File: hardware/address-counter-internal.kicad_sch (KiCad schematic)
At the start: 10 parts, among them U3 74LV163, U4 74LV163, U5 74LV163, U6 74LV163, U7 74LV163

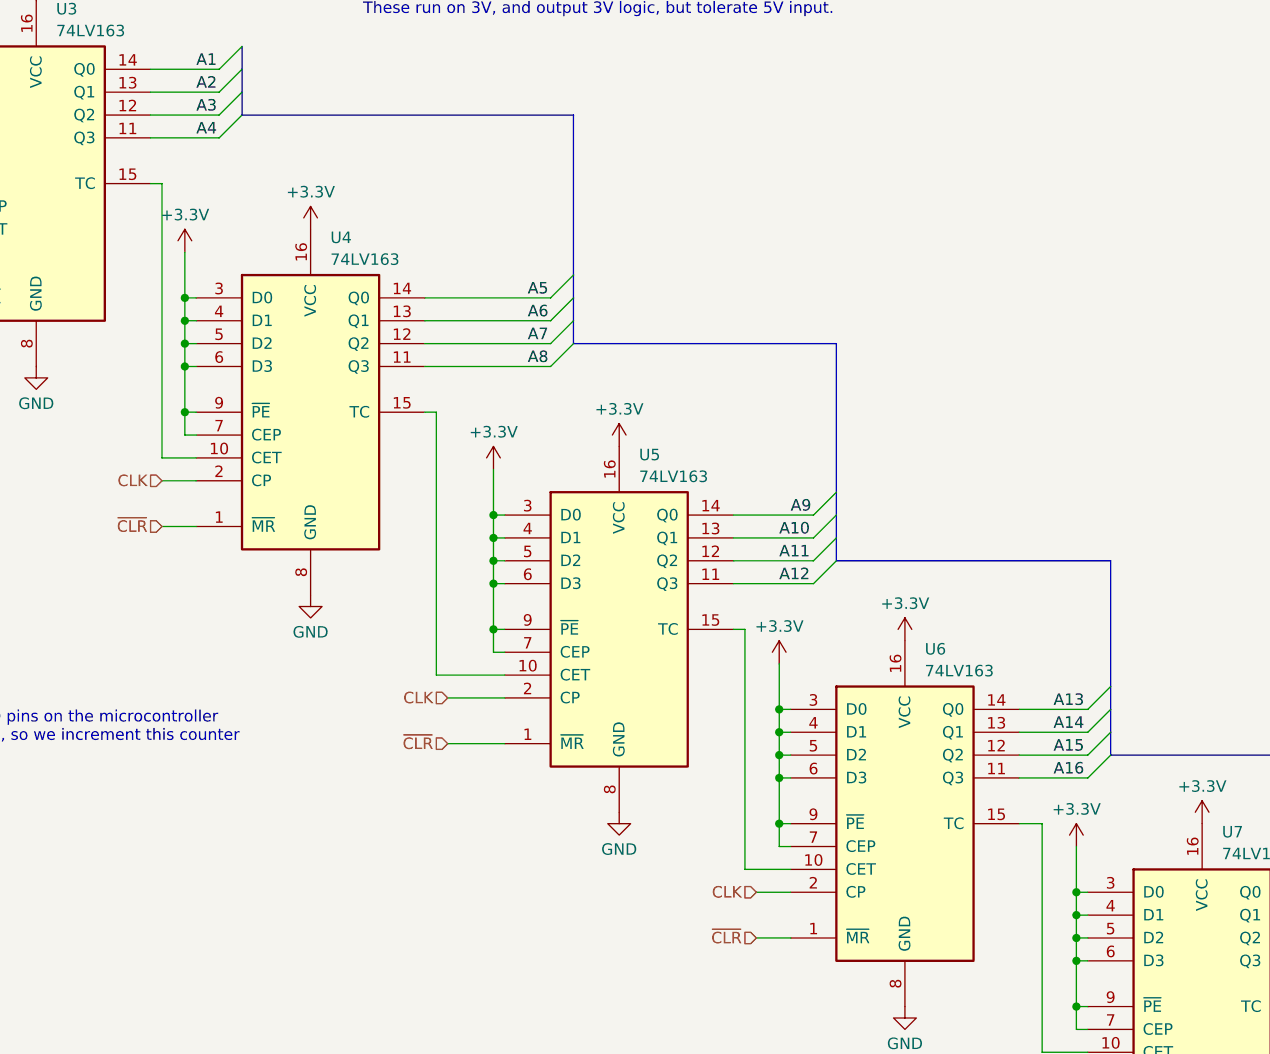
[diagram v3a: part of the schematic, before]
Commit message: Simplify microcontroller board BOM
Replace 74LV1T125 with 74LVC2G125, which simplifies the BOM by removing one special part.
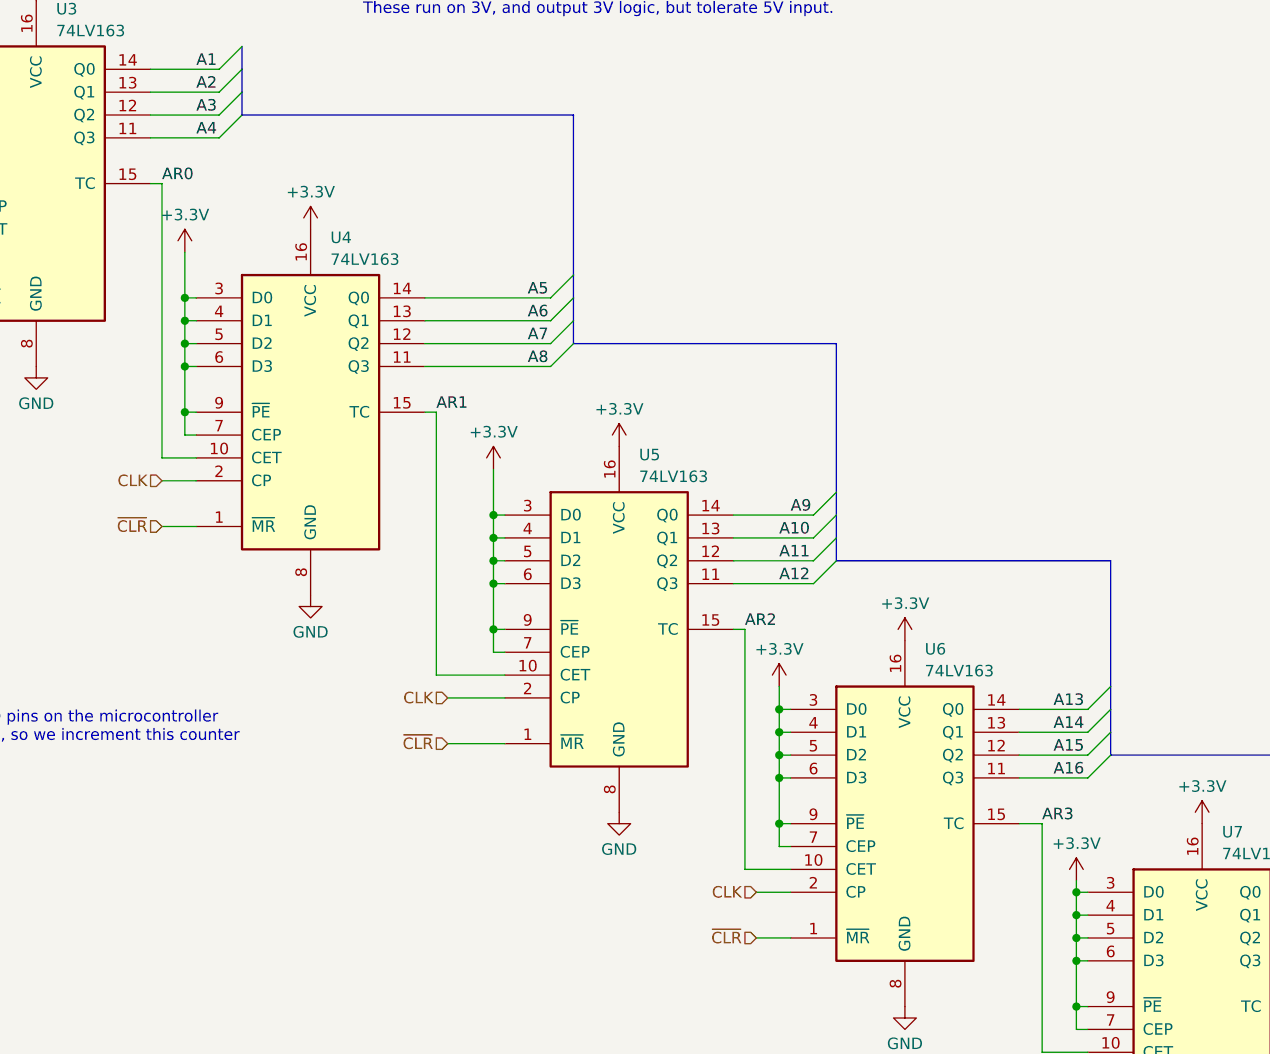
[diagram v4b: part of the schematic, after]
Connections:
- net AR0: now reaches U3.15 (TC), U4.10 (CET)
- net AR1: now reaches U4.15 (TC), U5.10 (CET)
- net AR2: now reaches U5.15 (TC), U6.10 (CET)
- net AR3: now reaches U6.15 (TC), U7.10 (CET)
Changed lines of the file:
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@@
 	(wire
 		(pts
-			(xy 163.83 115.57) (xy 163.83 120.65)
+			(xy 163.83 119.38) (xy 163.83 120.65)
 		)
 		(stroke
@@
 	(wire
 		(pts
-			(xy 130.81 95.25) (xy 130.81 100.33)
+			(xy 130.81 97.79) (xy 130.81 100.33)
 		)
 		(stroke
@@
 		)
 	)
+	(label "AR3"
+		(at 160.02 113.03 0)
+		(fields_autoplaced yes)
+		(effects
+			(font
+				(size 1.27 1.27)
+			)
+			(justify left bottom)
+		)
+	)
 	(label "A16"
 		(at 161.29 107.95 0)
@@
 		)
 	)
+	(label "AR1"
+		(at 92.71 67.31 0)
+		(fields_autoplaced yes)
+		(effects
+			(font
+				(size 1.27 1.27)
+			)
+			(justify left bottom)
+		)
+	)
 	(label "A10"
 		(at 130.81 81.28 0)
@@
 		)
 	)
+	(label "AR2"
+		(at 127 91.44 0)
+		(fields_autoplaced yes)
+		(effects
+			(font
+				(size 1.27 1.27)
+			)
+			(justify left bottom)
+		)
+	)
 	(label "A7"
 		(at 102.87 59.69 0)
@@
 	(label "A15"
 		(at 161.29 105.41 0)
+		(fields_autoplaced yes)
+		(effects
+			(font
+				(size 1.27 1.27)
+			)
+			(justify left bottom)
+		)
+	)
+	(label "AR0"
+		(at 62.23 41.91 0)
 		(fields_autoplaced yes)
 		(effects
@@
 	(symbol
 		(lib_id "power:+3.3V")
-		(at 130.81 95.25 0)
+		(at 130.81 97.79 0)
 		(unit 1)
 		(exclude_from_sim no)
@@
 		(fields_autoplaced yes)
 		(property "Reference" "#PWR038"
-			(at 130.81 99.06 0)
+			(at 130.81 101.6 0)
 			(effects
 				(font
@@
 		)
 		(property "Value" "+3.3V"
-			(at 130.81 91.1169 0)
+			(at 130.81 93.6569 0)
 			(effects
 				(font
@@
 		)
 		(property "Footprint" ""
-			(at 130.81 95.25 0)
+			(at 130.81 97.79 0)
 			(effects
 				(font
@@
 		)
 		(property "Datasheet" ""
-			(at 130.81 95.25 0)
+			(at 130.81 97.79 0)
 			(effects
 				(font
@@
 		)
 		(property "Description" "Power symbol creates a global label with name \"+3.3V\""
-			(at 130.81 95.25 0)
+			(at 130.81 97.79 0)
 			(effects
 				(font
@@
 	(symbol
 		(lib_id "power:+3.3V")
-		(at 163.83 115.57 0)
+		(at 163.83 119.38 0)
 		(unit 1)
 		(exclude_from_sim no)
@@
 		(fields_autoplaced yes)
 		(property "Reference" "#PWR039"
+			(at 163.83 123.19 0)
+			(effects
+				(font
+					(size 1.27 1.27)
+				)
+				(hide yes)
+			)
+		)
+		(property "Value" "+3.3V"
+			(at 163.83 115.2469 0)
+			(effects
+				(font
+					(size 1.27 1.27)
+				)
+			)
+		)
+		(property "Footprint" ""
 			(at 163.83 119.38 0)
 			(effects
@@
 			)
 		)
-		(property "Value" "+3.3V"
-			(at 163.83 111.4369 0)
-			(effects
-				(font
-					(size 1.27 1.27)
-				)
-			)
-		)
-		(property "Footprint" ""
-			(at 163.83 115.57 0)
-			(effects
-				(font
-					(size 1.27 1.27)
-				)
-				(hide yes)
-			)
-		)
 		(property "Datasheet" ""
-			(at 163.83 115.57 0)
+			(at 163.83 119.38 0)
 			(effects
 				(font
@@
 		)
 		(property "Description" "Power symbol creates a global label with name \"+3.3V\""
-			(at 163.83 115.57 0)
-			(effects
-				(font
+			(at 163.83 119.38 0)
+			(effects
+				(font

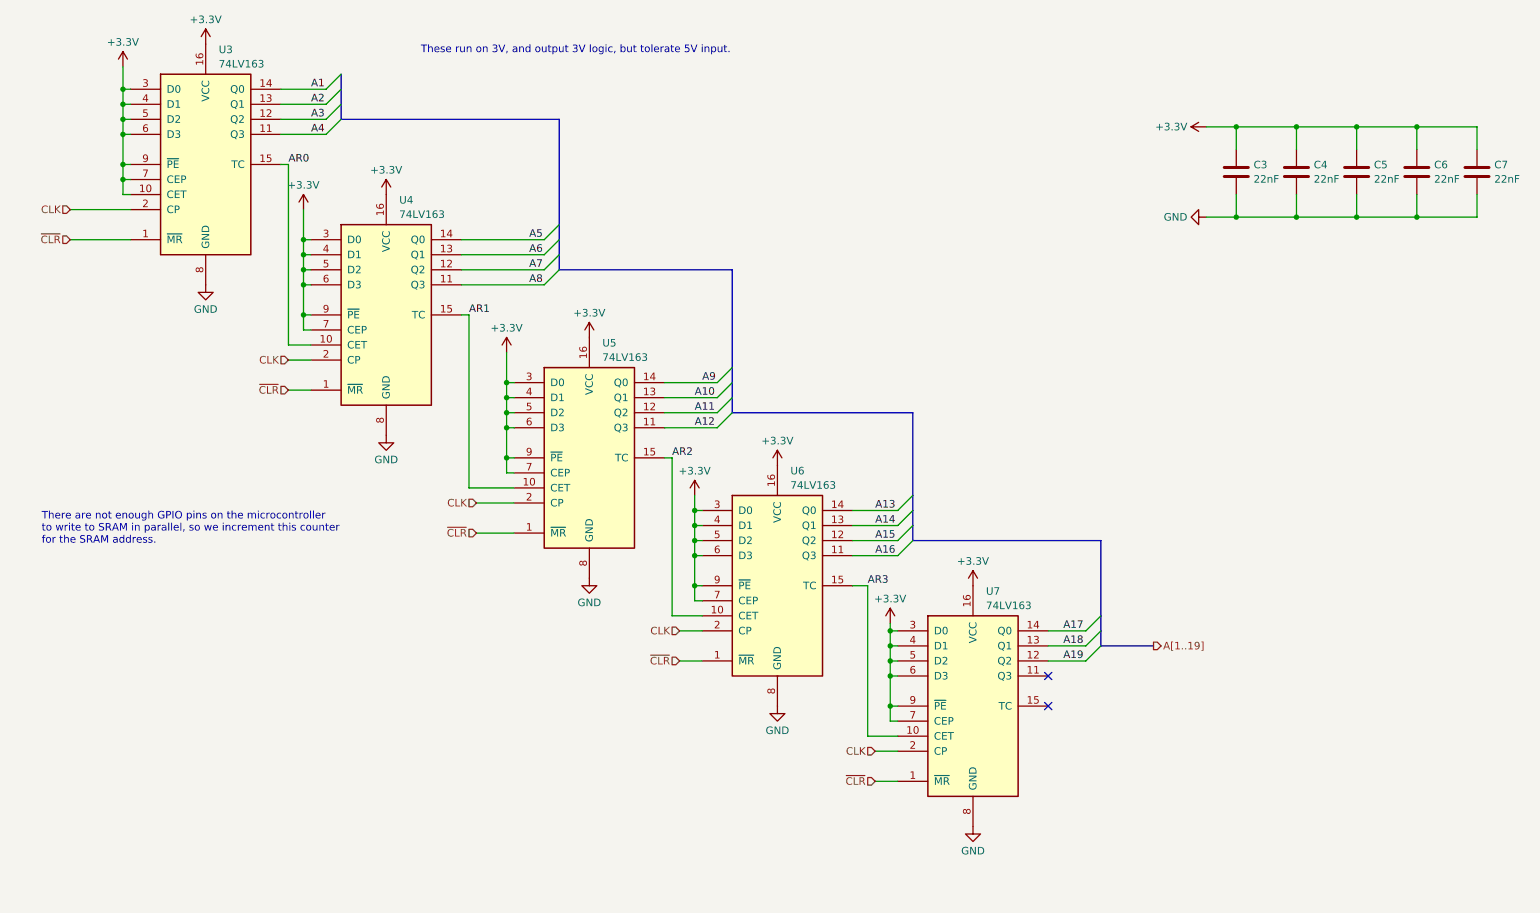
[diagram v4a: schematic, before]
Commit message: Improve uC board assembly process, fix minor bug
Changes to part numbers to better align with JLCPCB stock:
 - Replace 74LV164PW,118 / C179331 with SN74LV164APWR / C403720
 - Replace SN74LV163APWR / C2675453 with SN74LV161APWR / C2649404
   - Original had sync clear, but this is async clear, which is a bug
     fix!
 - Fix rotation of U8, U9, U13
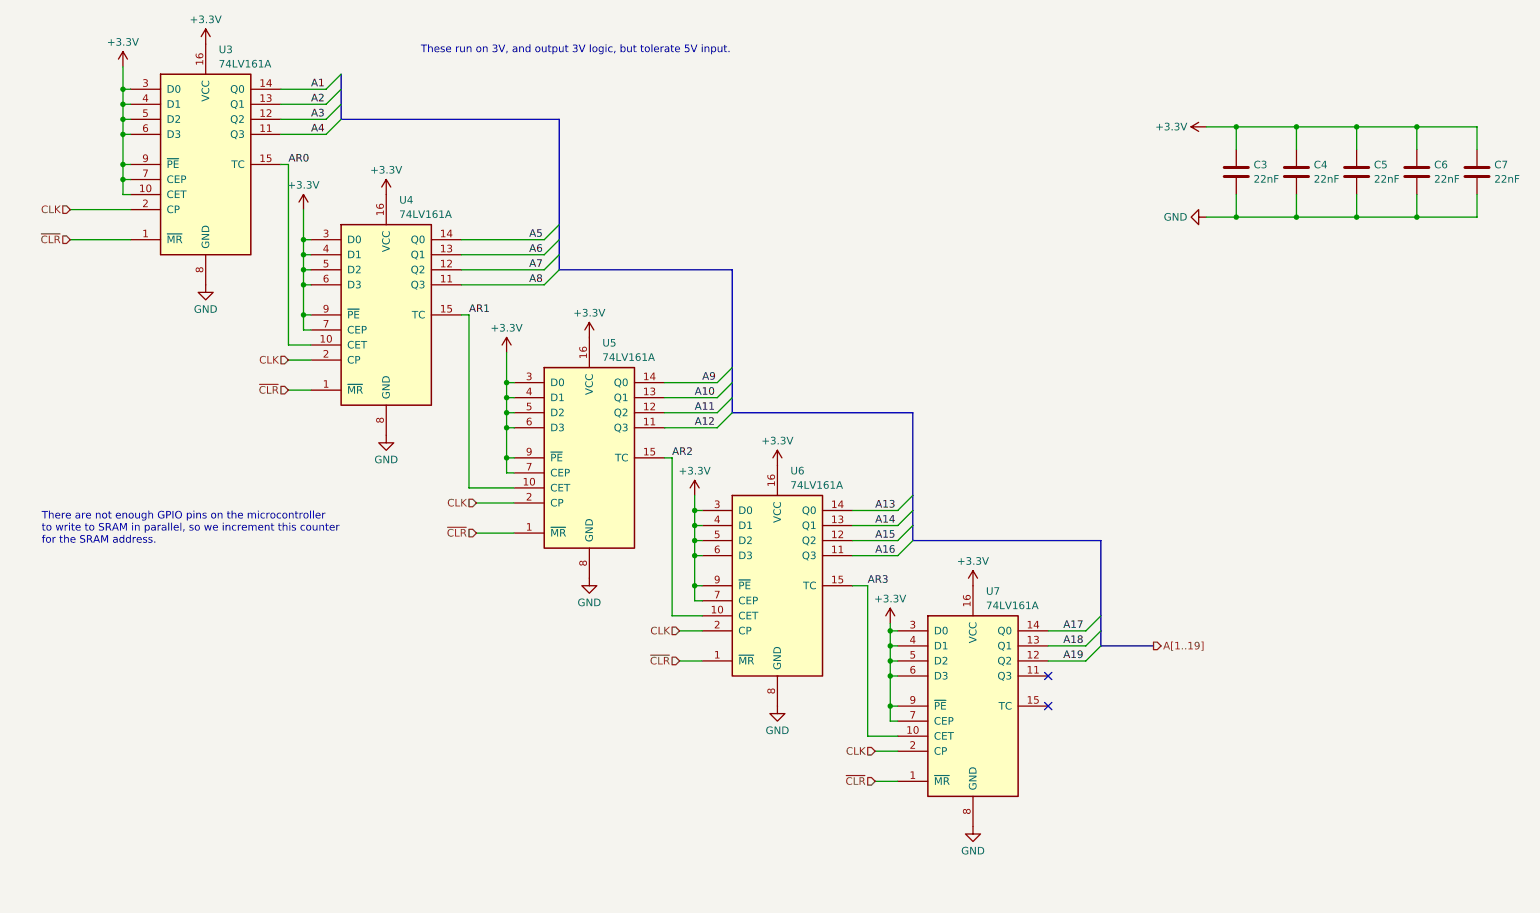
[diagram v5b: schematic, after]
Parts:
- U3, U4, U5, U6, U7: value 74LV163 -> 74LV161A; symbol 74xx:74LS163 -> 74xx:74LS161; JLCPCB Part Number C2675453 -> C2649404; Mouser Part Number 595-SN74LV163APWR -> 595-SN74LV161APWR; Part Number SN74LV163APWR -> SN74LV161APWR
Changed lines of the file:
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@@
 	)
 	(symbol
-		(lib_id "74xx:74LS163")
+		(lib_id "74xx:74LS161")
 		(at 78.74 67.31 0)
 		(unit 1)
@@
 			)
 		)
-		(property "Value" "74LV163"
+		(property "Value" "74LV161A"
 			(at 80.9341 50.3498 0)
 			(effects
@@
 			)
 		)
-		(property "Datasheet" "https://www.ti.com/lit/gpn/sn74lv163a"
+		(property "Datasheet" "https://www.ti.com/lit/gpn/sn74lv161a"
 			(at 78.74 67.31 0)
 			(effects
@@
 			)
 		)
-		(property "Mouser Part Number" "595-SN74LV163APWR"
+		(property "Mouser Part Number" "595-SN74LV161APWR"
 			(at 78.74 67.31 0)
 			(effects
@@
 			)
 		)
-		(property "Part Number" "SN74LV163APWR"
+		(property "Part Number" "SN74LV161APWR"
 			(at 78.74 67.31 0)
 			(effects
@@
 			)
 		)
-		(property "JLCPCB Part Number" "C2675453"
+		(property "JLCPCB Part Number" "C2649404"
 			(at 78.74 67.31 0)
 			(effects
@@
 	)
 	(symbol
-		(lib_id "74xx:74LS163")
+		(lib_id "74xx:74LS161")
 		(at 144.78 113.03 0)
 		(unit 1)
@@
 			)
 		)
-		(property "Value" "74LV163"
+		(property "Value" "74LV161A"
 			(at 146.9741 96.0698 0)
 			(effects
@@
 			)
 		)
-		(property "Datasheet" "https://www.ti.com/lit/gpn/sn74lv163a"
+		(property "Datasheet" "https://www.ti.com/lit/gpn/sn74lv161a"
 			(at 144.78 113.03 0)
 			(effects
@@
 			)
 		)
-		(property "Mouser Part Number" "595-SN74LV163APWR"
+		(property "Mouser Part Number" "595-SN74LV161APWR"
 			(at 144.78 113.03 0)
 			(effects
@@
 			)
 		)
-		(property "Part Number" "SN74LV163APWR"
+		(property "Part Number" "SN74LV161APWR"
 			(at 144.78 113.03 0)
 			(effects
@@
 			)
 		)
-		(property "JLCPCB Part Number" "C2675453"
+		(property "JLCPCB Part Number" "C2649404"
 			(at 144.78 113.03 0)
 			(effects
@@
 	)
 	(symbol
-		(lib_id "74xx:74LS163")
+		(lib_id "74xx:74LS161")
 		(at 177.8 133.35 0)
 		(unit 1)
@@
 			)
 		)
-		(property "Value" "74LV163"
+		(property "Value" "74LV161A"
 			(at 179.9941 116.3898 0)
 			(effects
@@
 			)
 		)
-		(property "Datasheet" "https://www.ti.com/lit/gpn/sn74lv163a"
+		(property "Datasheet" "https://www.ti.com/lit/gpn/sn74lv161a"
 			(at 177.8 133.35 0)
 			(effects
@@
 			)
 		)
-		(property "Mouser Part Number" "595-SN74LV163APWR"
+		(property "Mouser Part Number" "595-SN74LV161APWR"
 			(at 177.8 133.35 0)
 			(effects
@@
 			)
 		)
-		(property "Part Number" "SN74LV163APWR"
+		(property "Part Number" "SN74LV161APWR"
 			(at 177.8 133.35 0)
 			(effects
@@
 			)
 		)
-		(property "JLCPCB Part Number" "C2675453"
+		(property "JLCPCB Part Number" "C2649404"
 			(at 177.8 133.35 0)
 			(effects
@@
 	)
 	(symbol
-		(lib_id "74xx:74LS163")
+		(lib_id "74xx:74LS161")
 		(at 48.26 41.91 0)
 		(unit 1)
@@
 			)
 		)
-		(property "Value" "74LV163"
+		(property "Value" "74LV161A"
 			(at 50.4541 24.9498 0)
 			(effects
@@
 			)
 		)
-		(property "Datasheet" "https://www.ti.com/lit/gpn/sn74lv163a"
+		(property "Datasheet" "https://www.ti.com/lit/gpn/sn74lv161a"
 			(at 48.26 41.91 0)
 			(effects
@@
 			)
 		)
-		(property "Mouser Part Number" "595-SN74LV163APWR"
+		(property "Mouser Part Number" "595-SN74LV161APWR"
 			(at 48.26 41.91 0)
 			(effects
@@
 			)
 		)
-		(property "Part Number" "SN74LV163APWR"
+		(property "Part Number" "SN74LV161APWR"
 			(at 48.26 41.91 0)
 			(effects
@@
 			)
 		)
-		(property "JLCPCB Part Number" "C2675453"
+		(property "JLCPCB Part Number" "C2649404"
 			(at 48.26 41.91 0)
 			(effects
@@
 	)
 	(symbol
-		(lib_id "74xx:74LS163")
+		(lib_id "74xx:74LS161")
 		(at 113.03 91.44 0)
 		(unit 1)
@@
 			)
 		)
-		(property "Value" "74LV163"
+		(property "Value" "74LV161A"
 			(at 115.2241 74.4798 0)
 			(effects
@@
 			)
 		)
-		(property "Datasheet" "https://www.ti.com/lit/gpn/sn74lv163a"
+		(property "Datasheet" "https://www.ti.com/lit/gpn/sn74lv161a"
 			(at 113.03 91.44 0)
 			(effects
@@
 			)
 		)
-		(property "Mouser Part Number" "595-SN74LV163APWR"
+		(property "Mouser Part Number" "595-SN74LV161APWR"
 			(at 113.03 91.44 0)
 			(effects
@@
 			)
 		)
-		(property "Part Number" "SN74LV163APWR"
+		(property "Part Number" "SN74LV161APWR"
 			(at 113.03 91.44 0)
 			(effects
@@
 			)
 		)
-		(property "JLCPCB Part Number" "C2675453"
+		(property "JLCPCB Part Number" "C2649404"
 			(at 113.03 91.44 0)
 			(effects
